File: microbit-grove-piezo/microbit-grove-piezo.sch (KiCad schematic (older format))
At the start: 6 parts, among them J1 microbit_smd_socket, J2 GROVE-CONNECTOR-SMD_4+2P-2.0_, J3 GROVE-CONNECTOR-SMD_4+2P-2.0_, J4 GROVE-CONNECTOR-SMD_4+2P-2.0_, J5 GROVE-CONNECTOR-SMD_4+2P-2.0_

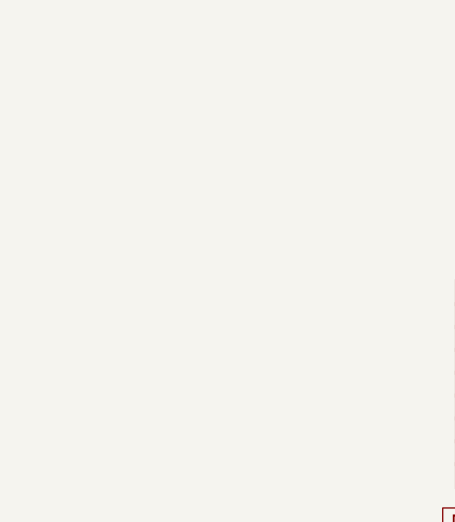
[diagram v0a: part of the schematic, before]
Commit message: Add logos to grove/piezo board
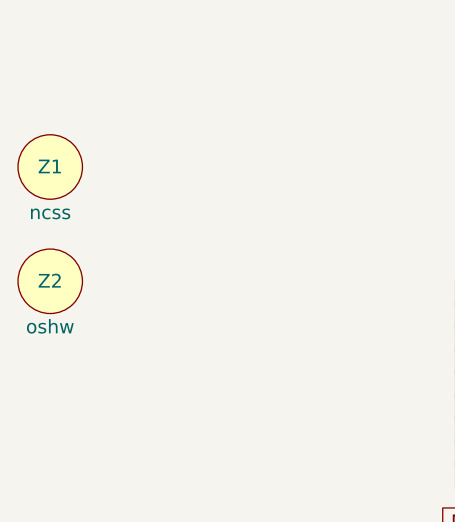
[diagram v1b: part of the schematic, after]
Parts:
- added Z1: ncss, logos:ncss, symbol symbol
- added Z2: oshw, logos:OSHW-Logo2_7.3x6mm_Copper, symbol symbol
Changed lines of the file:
@@
 LIBS:microbit-socket
 LIBS:seeed-opl-connector
+LIBS:symbol
 LIBS:microbit-grove-piezo-cache
 EELAYER 25 0
@@
 NoConn ~ 8250 5150
 NoConn ~ 8250 5750
+$Comp
+L symbol Z1
+U 1 1 5A1EB7CF
+P 2200 3350
+F 0 "Z1" H 2200 3350 60  0000 C CNN
+F 1 "ncss" H 2200 3150 60  0000 C CNN
+F 2 "logos:ncss" H 2200 3350 60  0001 C CNN
+F 3 "" H 2200 3350 60  0001 C CNN
+	1    2200 3350
+	1    0    0    -1
+$EndComp
+$Comp
+L symbol Z2
+U 1 1 5A1EB880
+P 2200 3850
+F 0 "Z2" H 2200 3850 60  0000 C CNN
+F 1 "oshw" H 2200 3650 60  0000 C CNN
+F 2 "logos:OSHW-Logo2_7.3x6mm_Copper" H 2200 3850 60  0001 C CNN
+F 3 "" H 2200 3850 60  0001 C CNN
+	1    2200 3850
+	1    0    0    -1
+$EndComp
 $EndSCHEMATC

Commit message: Make small logos for the grove board.
Test run gerbers.
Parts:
- Z1: footprint logos:ncss -> logos:ncss_small
- Z2: footprint logos:OSHW-Logo2_7.3x6mm_Copper -> logos:OSHW-Logo2_7.3x6mm_Copper_NoText
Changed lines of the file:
@@
 F 0 "Z1" H 2200 3350 60  0000 C CNN
 F 1 "ncss" H 2200 3150 60  0000 C CNN
-F 2 "logos:ncss" H 2200 3350 60  0001 C CNN
+F 2 "logos:ncss_small" H 2200 3350 60  0001 C CNN
 F 3 "" H 2200 3350 60  0001 C CNN
 	1    2200 3350
@@
 F 0 "Z2" H 2200 3850 60  0000 C CNN
 F 1 "oshw" H 2200 3650 60  0000 C CNN
-F 2 "logos:OSHW-Logo2_7.3x6mm_Copper" H 2200 3850 60  0001 C CNN
+F 2 "logos:OSHW-Logo2_7.3x6mm_Copper_NoText" H 2200 3850 60  0001 C CNN
 F 3 "" H 2200 3850 60  0001 C CNN
 	1    2200 3850

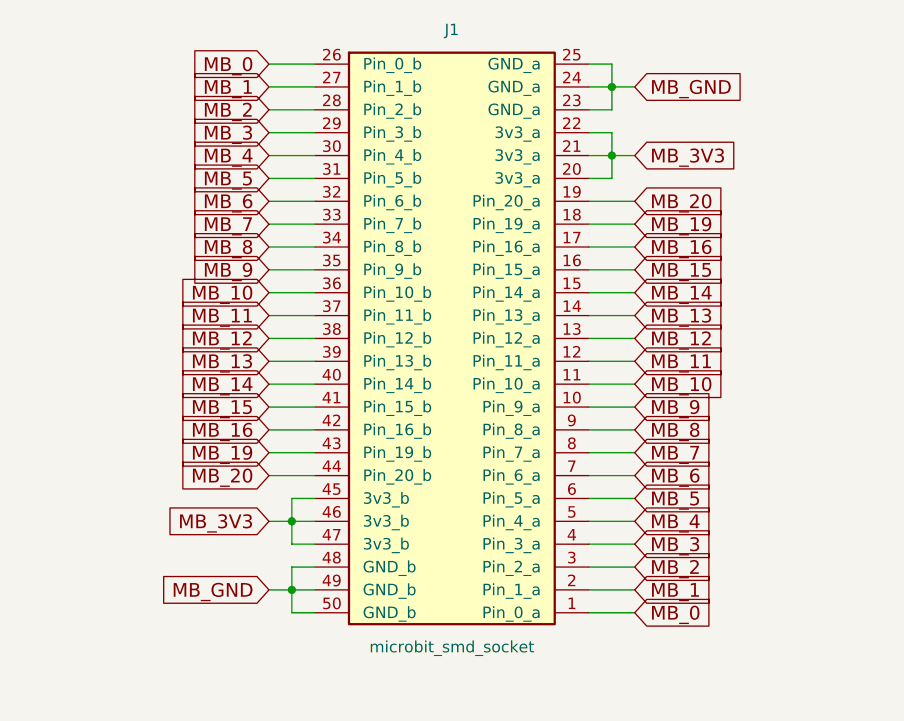
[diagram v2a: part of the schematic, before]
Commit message: Replace vcc/gnd with pours.
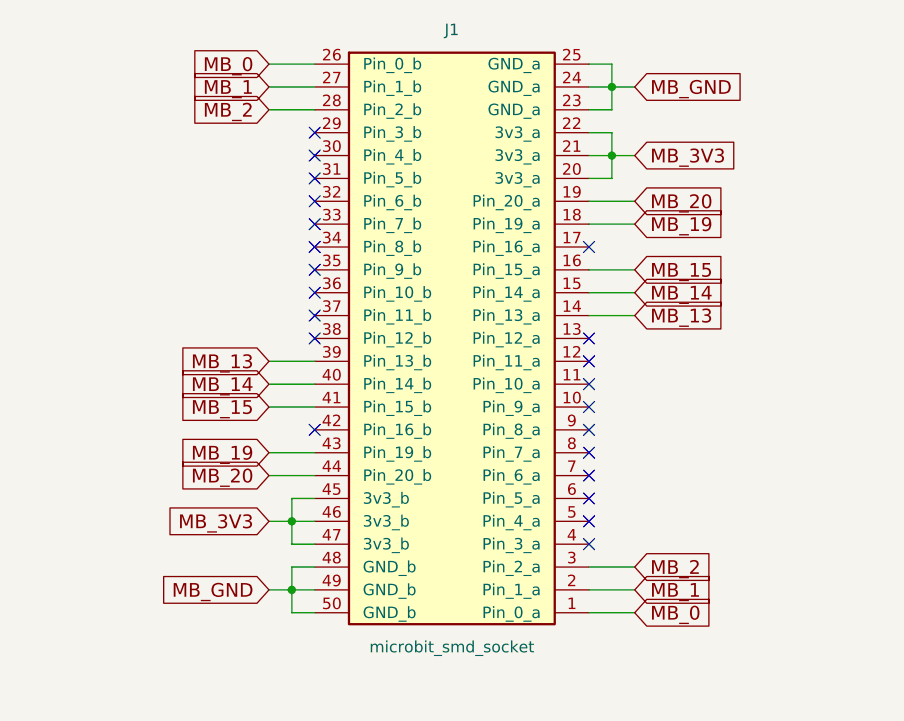
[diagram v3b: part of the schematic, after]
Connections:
- net MB_10: no longer names the net of J1.11 (Pin_10_a)
- net MB_10: no longer J1.36 (Pin_10_b)
- net MB_11: no longer names the net of J1.12 (Pin_11_a)
- net MB_11: no longer J1.37 (Pin_11_b)
- net MB_12: no longer names the net of J1.13 (Pin_12_a)
- net MB_12: no longer J1.38 (Pin_12_b)
- net MB_16: no longer names the net of J1.17 (Pin_16_a)
- net MB_16: no longer J1.42 (Pin_16_b)
- net MB_3: no longer names the net of J1.29 (Pin_3_b)
- net MB_3: no longer J1.4 (Pin_3_a)
- net MB_4: no longer names the net of J1.30 (Pin_4_b)
- net MB_4: no longer J1.5 (Pin_4_a)
- net MB_5: no longer names the net of J1.31 (Pin_5_b)
- net MB_5: no longer J1.6 (Pin_5_a)
- net MB_6: no longer names the net of J1.32 (Pin_6_b)
- net MB_6: no longer J1.7 (Pin_6_a)
- net MB_7: no longer names the net of J1.33 (Pin_7_b)
- net MB_7: no longer J1.8 (Pin_7_a)
- net MB_8: no longer names the net of J1.34 (Pin_8_b)
- net MB_8: no longer J1.9 (Pin_8_a)
- net MB_9: no longer names the net of J1.10 (Pin_9_a)
- net MB_9: no longer J1.35 (Pin_9_b)
- no-connect marks 8 -> 30
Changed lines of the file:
@@
 Text GLabel 5950 3600 2    60   Input ~ 0
 MB_19
-Text GLabel 5950 3700 2    60   Input ~ 0
-MB_16
 Text GLabel 5950 3800 2    60   Input ~ 0
 MB_15
@@
 Text GLabel 5950 4000 2    60   Input ~ 0
 MB_13
-Text GLabel 5950 4100 2    60   Input ~ 0
-MB_12
-Text GLabel 5950 4200 2    60   Input ~ 0
-MB_11
-Text GLabel 5950 4300 2    60   Input ~ 0
-MB_10
-Text GLabel 5950 4400 2    60   Input ~ 0
-MB_9
-Text GLabel 5950 4500 2    60   Input ~ 0
-MB_8
-Text GLabel 5950 4600 2    60   Input ~ 0
-MB_7
-Text GLabel 5950 4700 2    60   Input ~ 0
-MB_6
-Text GLabel 5950 4800 2    60   Input ~ 0
-MB_5
-Text GLabel 5950 4900 2    60   Input ~ 0
-MB_4
-Text GLabel 5950 5000 2    60   Input ~ 0
-MB_3
 Text GLabel 5950 5100 2    60   Input ~ 0
 MB_2
@@
 	5950 3600 5750 3600
 Wire Wire Line
-	5750 3700 5950 3700
-Wire Wire Line
 	5950 3800 5750 3800
 Wire Wire Line
@@
 Wire Wire Line
 	5950 4000 5750 4000
-Wire Wire Line
-	5750 4100 5950 4100
-Wire Wire Line
-	5950 4200 5750 4200
-Wire Wire Line
-	5750 4300 5950 4300
-Wire Wire Line
-	5950 4400 5750 4400
-Wire Wire Line
-	5750 4500 5950 4500
-Wire Wire Line
-	5950 4600 5750 4600
-Wire Wire Line
-	5750 4700 5950 4700
-Wire Wire Line
-	5950 4800 5750 4800
-Wire Wire Line
-	5750 4900 5950 4900
-Wire Wire Line
-	5950 5000 5750 5000
 Wire Wire Line
 	5750 5100 5950 5100
@@
 Text GLabel 4350 4600 0    60   Input ~ 0
 MB_19
-Text GLabel 4350 4500 0    60   Input ~ 0
-MB_16
 Text GLabel 4350 4400 0    60   Input ~ 0
 MB_15
@@
 Text GLabel 4350 4200 0    60   Input ~ 0
 MB_13
-Text GLabel 4350 4100 0    60   Input ~ 0
-MB_12
-Text GLabel 4350 4000 0    60   Input ~ 0
-MB_11
-Text GLabel 4350 3900 0    60   Input ~ 0
-MB_10
-Text GLabel 4350 3800 0    60   Input ~ 0
-MB_9
-Text GLabel 4350 3700 0    60   Input ~ 0
-MB_8
-Text GLabel 4350 3600 0    60   Input ~ 0
-MB_7
-Text GLabel 4350 3500 0    60   Input ~ 0
-MB_6
-Text GLabel 4350 3400 0    60   Input ~ 0
-MB_5
-Text GLabel 4350 3300 0    60   Input ~ 0
-MB_4
-Text GLabel 4350 3200 0    60   Input ~ 0
-MB_3
 Text GLabel 4350 3100 0    60   Input ~ 0
 MB_2
@@
 	4350 4600 4550 4600
 Wire Wire Line
-	4550 4500 4350 4500
-Wire Wire Line
 	4350 4400 4550 4400
 Wire Wire Line
@@
 Wire Wire Line
 	4350 4200 4550 4200
-Wire Wire Line
-	4550 4100 4350 4100
-Wire Wire Line
-	4350 4000 4550 4000
-Wire Wire Line
-	4550 3900 4350 3900
-Wire Wire Line
-	4350 3800 4550 3800
-Wire Wire Line
-	4550 3700 4350 3700
-Wire Wire Line
-	4350 3600 4550 3600
-Wire Wire Line
-	4550 3500 4350 3500
-Wire Wire Line
-	4350 3400 4550 3400
-Wire Wire Line
-	4550 3300 4350 3300
-Wire Wire Line
-	4350 3200 4550 3200
 Wire Wire Line
 	4550 3100 4350 3100
@@
 	1    0    0    -1
 $EndComp
+NoConn ~ 5750 3700
+NoConn ~ 5750 4100
+NoConn ~ 5750 4200
+NoConn ~ 5750 4300
+NoConn ~ 5750 4400
+NoConn ~ 5750 4500
+NoConn ~ 5750 4600
+NoConn ~ 5750 4700
+NoConn ~ 5750 4800
+NoConn ~ 5750 4900
+NoConn ~ 4550 3300
+NoConn ~ 4550 3400
+NoConn ~ 4550 3500
+NoConn ~ 4550 3600
+NoConn ~ 4550 3700
+NoConn ~ 4550 3800
+NoConn ~ 4550 3900
+NoConn ~ 4550 4000
+NoConn ~ 4550 4100
+NoConn ~ 4550 4500
+NoConn ~ 5750 5000
+NoConn ~ 4550 3200
 $EndSCHEMATC
